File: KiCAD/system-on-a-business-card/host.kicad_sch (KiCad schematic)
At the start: 27 parts, among them Q1 2N7002K, Q2 2N7002K, SW2 SW_Push, U2 ESP32-C3, U3 ZD25WQ32C, Y1 40MHz

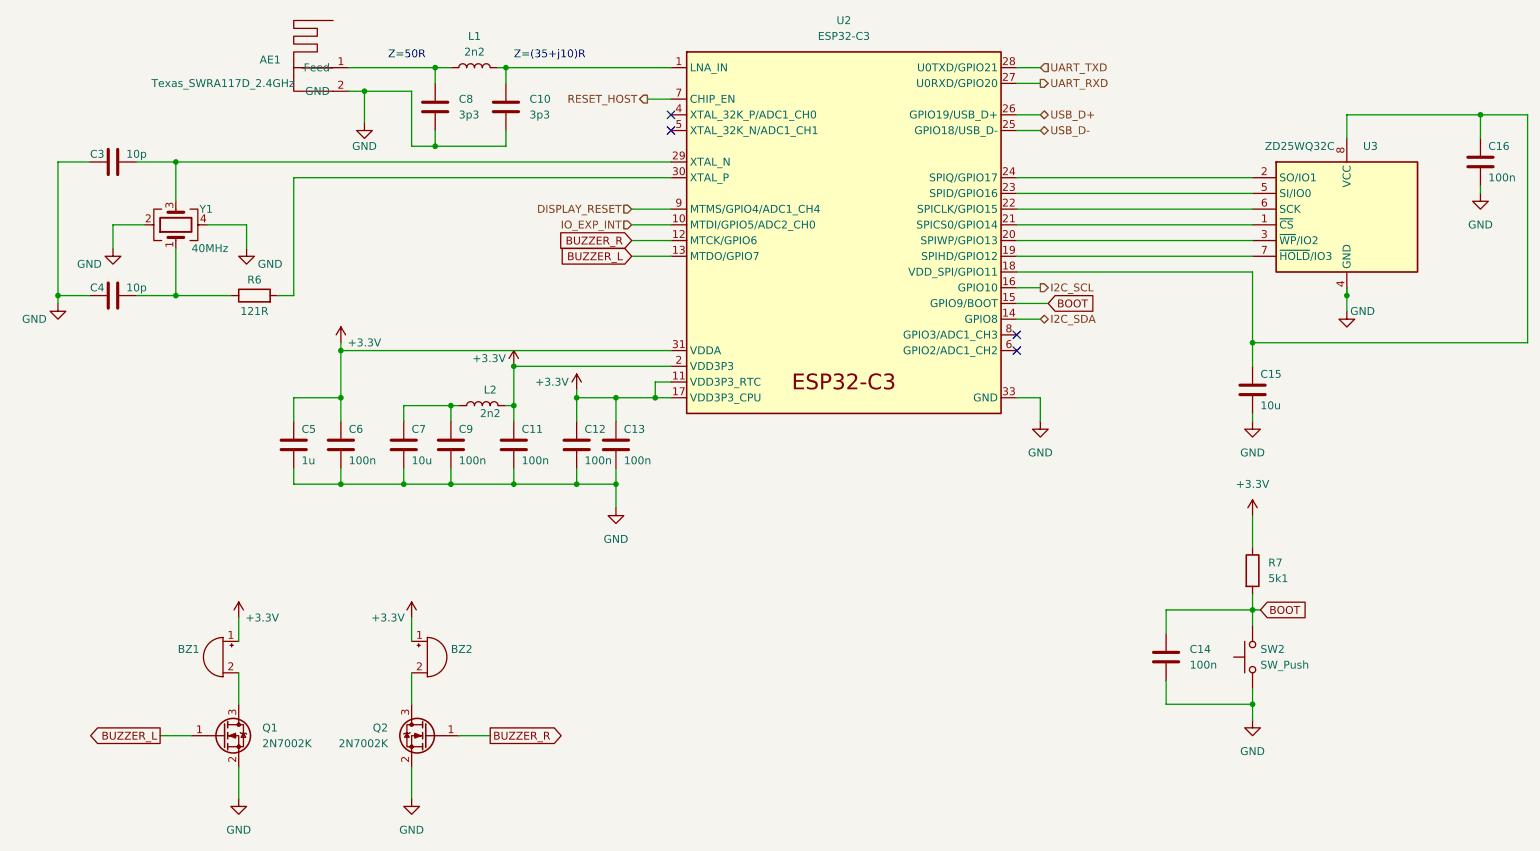
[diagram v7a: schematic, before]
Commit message: #10: added micro sd card
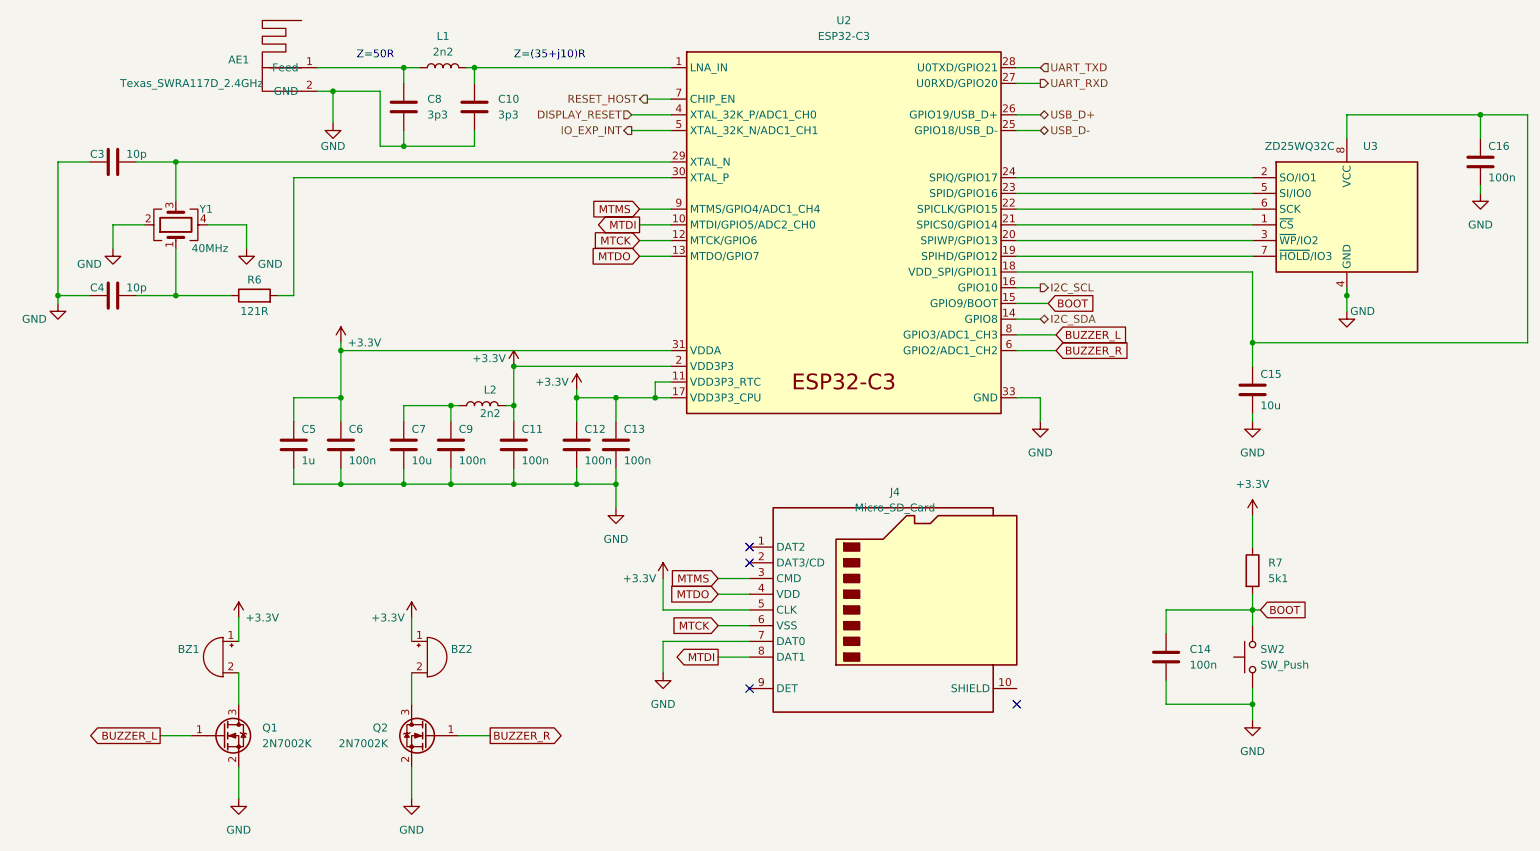
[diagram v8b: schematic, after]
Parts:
- added J4: Micro_SD_Card, Prj_connector_card:microSD_HC_Hanbo_Electronic_TF-018B-H15, symbol Connector:Micro_SD_Card_Det1
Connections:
- net +3.3V: now also J4.5 (CLK)
- net BUZZER_L: now also U2.8 (GPIO3/ADC1_CH3); no longer U2.13 (MTDO/GPIO7)
- net BUZZER_R: now also U2.6 (GPIO2/ADC1_CH2); no longer U2.12 (MTCK/GPIO6)
- net DISPLAY_RESET: now also U2.4 (XTAL_32K_P/ADC1_CH0); no longer U2.9 (MTMS/GPIO4/ADC1_CH4)
- net GND: now also J4.7 (DAT0)
- net IO_EXP_INT: now also U2.5 (XTAL_32K_N/ADC1_CH1); no longer U2.10 (MTDI/GPIO5/ADC2_CH0)
- new net MTCK: J4.6 (VSS), U2.12 (MTCK/GPIO6)
- new net MTDI: J4.8 (DAT1), U2.10 (MTDI/GPIO5/ADC2_CH0)
- new net MTDO: J4.4 (VDD), U2.13 (MTDO/GPIO7)
- new net MTMS: J4.3 (CMD), U2.9 (MTMS/GPIO4/ADC1_CH4)
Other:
- moved on the sheet: AE1, C10, C8, L1
